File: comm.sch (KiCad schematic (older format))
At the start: 18 parts

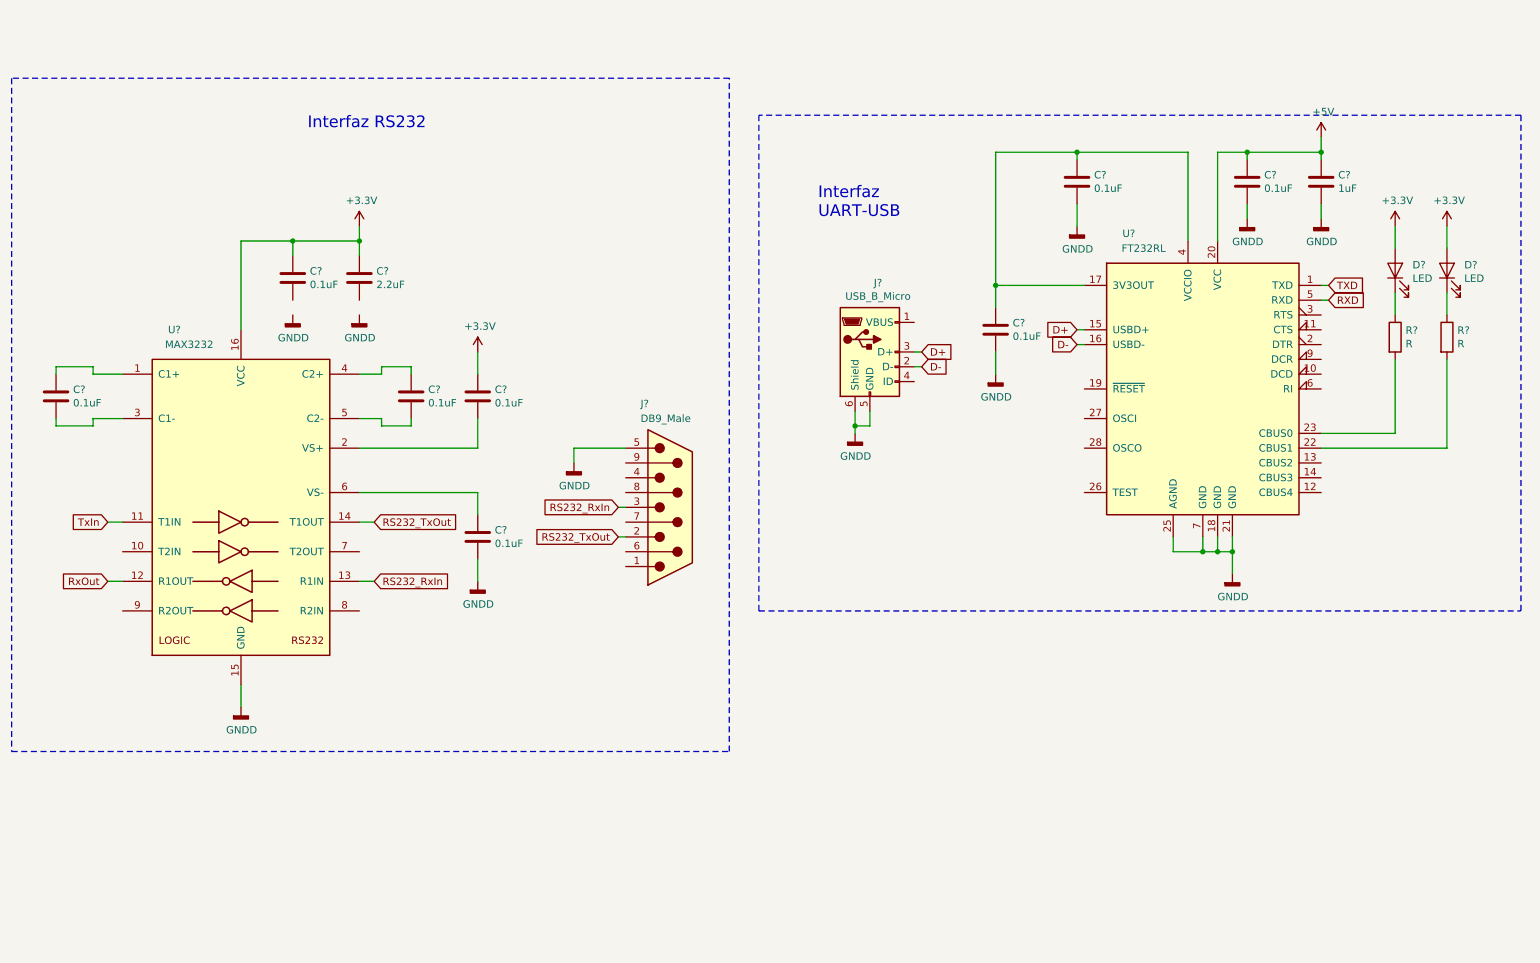
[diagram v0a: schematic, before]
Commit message: Se hace cambios en el esquematico y se anexa PCB
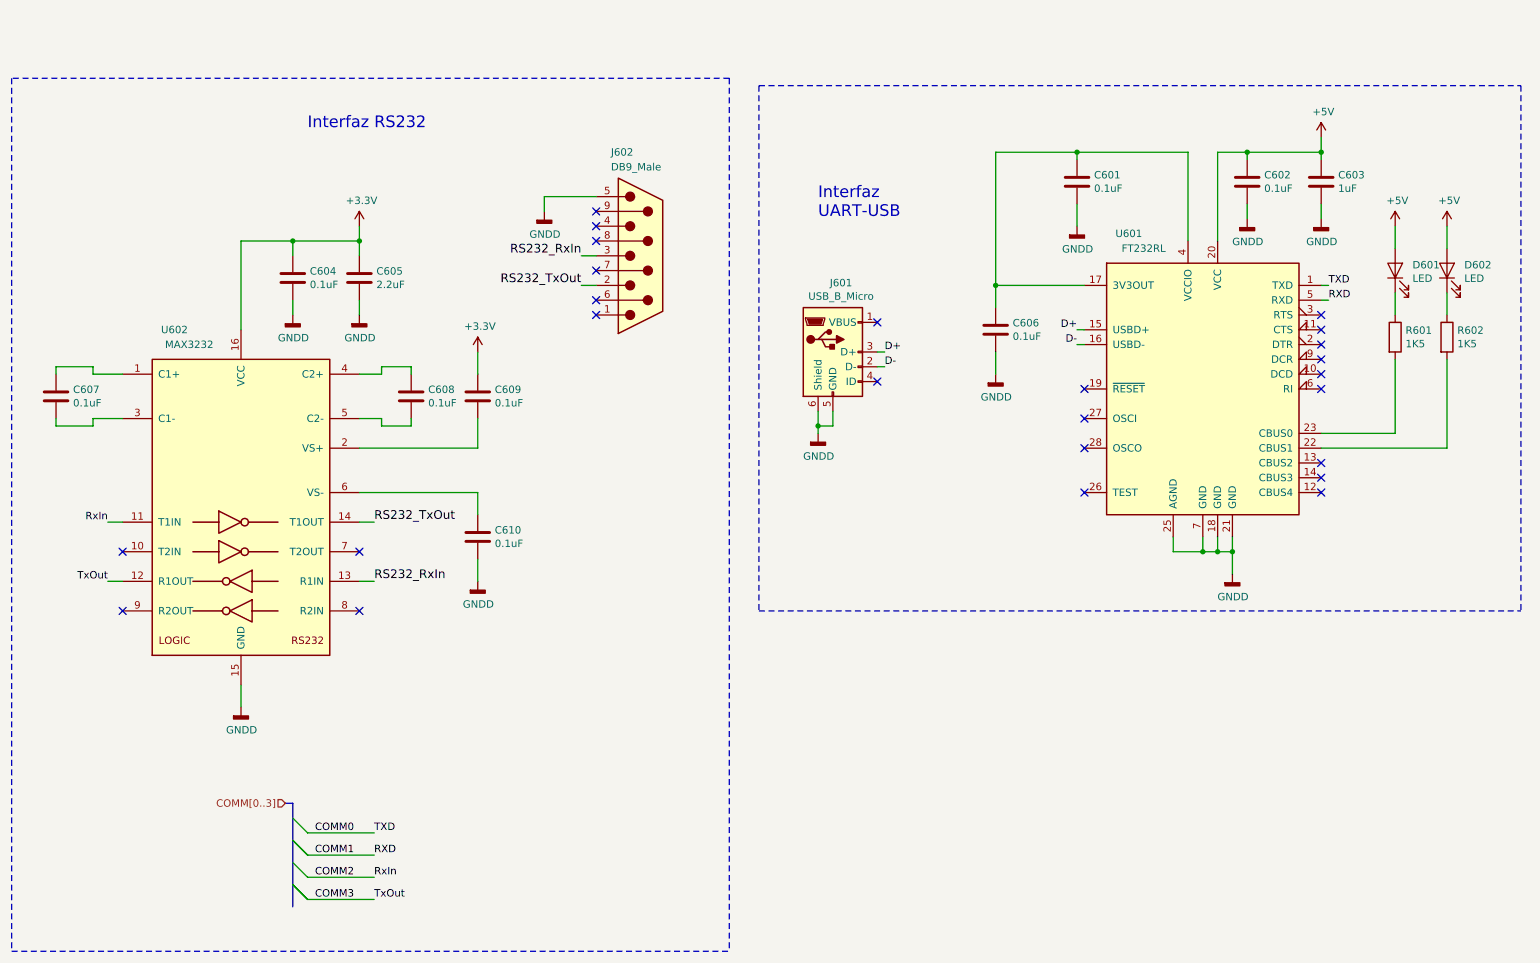
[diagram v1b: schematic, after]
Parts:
- C601, C602, C603, C604, C606, C607, C608, C609, C610: renamed from C?; footprint (none) -> Capacitor_SMD:C_0805_2012Metric_Pad1.15x1.40mm_HandSolder
- C605: renamed from C?; footprint (none) -> Capacitor_SMD:C_1206_3216Metric_Pad1.42x1.75mm_HandSolder
- D601, D602: renamed from D?; footprint (none) -> LED_SMD:LED_0805_2012Metric_Pad1.15x1.40mm_HandSolder
- J601: renamed from J?; footprint (none) -> Connector_USB:USB_Micro-B_Molex_47346-0001
- J602: renamed from J?; footprint (none) -> Connector_Dsub:DSUB-9_Male_Horizontal_P2.77x2.84mm_EdgePinOffset7.70mm_Housed_MountingHolesOffset9.12mm
- R601, R602: renamed from R?; value R -> 1K5; footprint (none) -> Resistor_SMD:R_0805_2012Metric_Pad1.15x1.40mm_HandSolder
- U602: renamed from U?; footprint (none) -> Package_SO:SOIC-16_3.9x9.9mm_P1.27mm
- gave numbers to parts that had none: 1
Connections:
- net +3V3: no longer D601.2 (A), D602.2 (A)
- net +5V: now also D601.2 (A), D602.2 (A)
- net GNDD: now also C604.2, C605.2
- net RXD renamed COMM1
- net RxOut renamed COMM3
- net TXD renamed COMM0
- net TxIn renamed COMM2
- no-connect marks 0 -> 25
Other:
- moved on the sheet: J601, J602

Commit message: Se realizan correcciones finales y se agregan carpetas BOM, Datasheet, Doc, Gerbers, lib.pretty y shapes3D
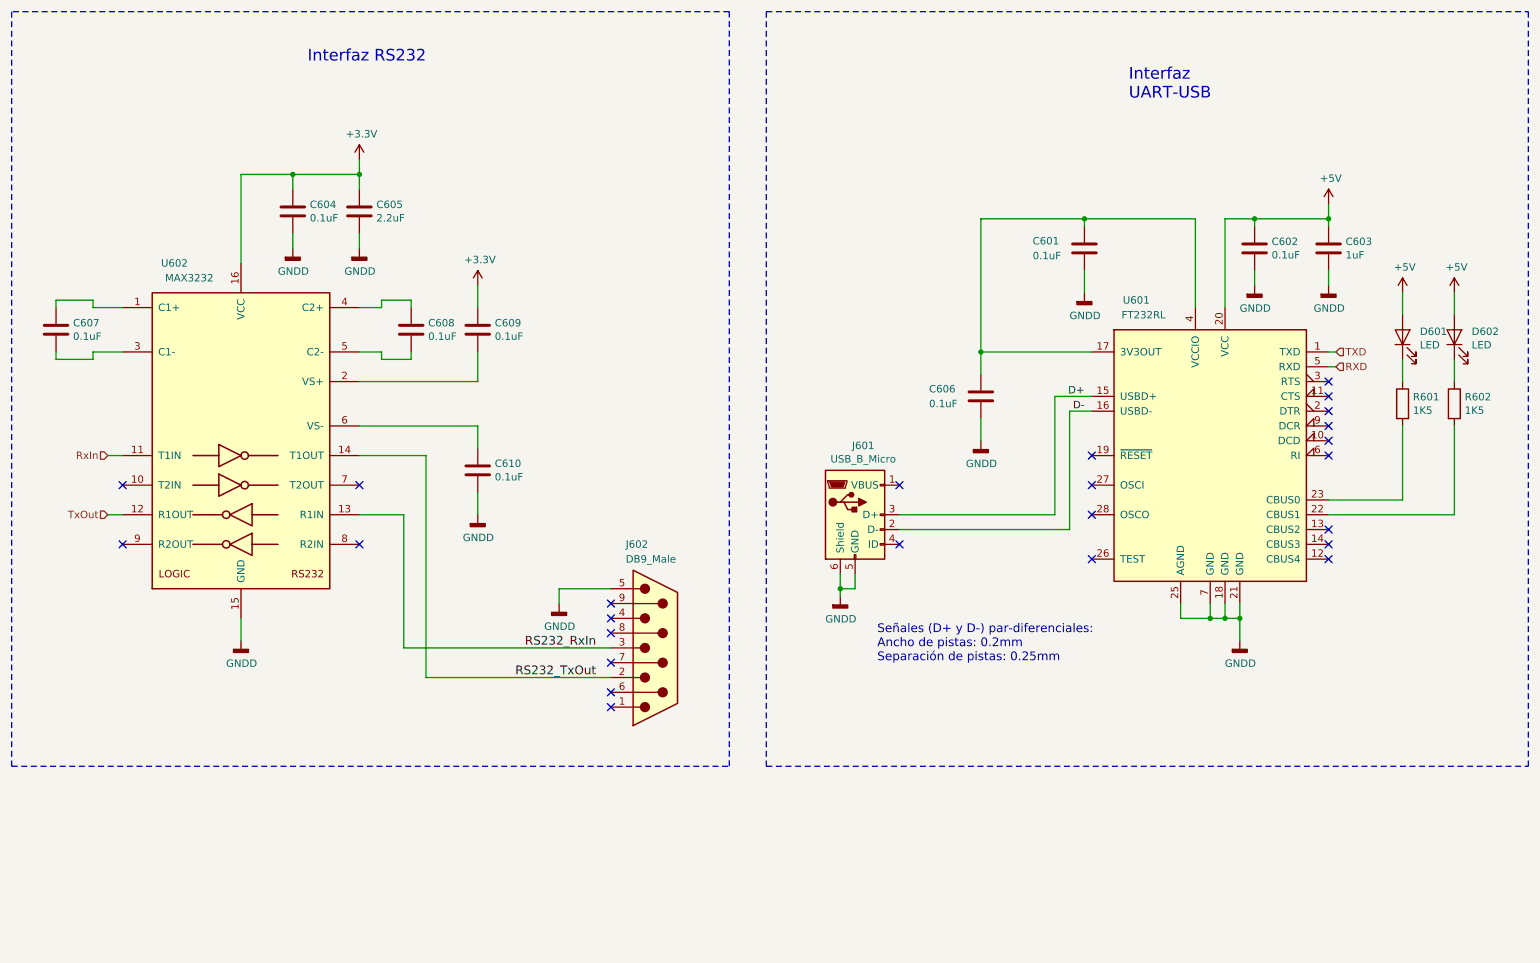
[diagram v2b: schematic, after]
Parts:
- J602: footprint Connector_Dsub:DSUB-9_Male_Horizontal_P2.77x2.84mm_EdgePinOffset7.70mm_Housed_MountingHolesOffset9.12mm -> Connector_Dsub:DSUB-9_Male_Horizontal_P2.77x2.84mm_EdgePinOffset4.94mm_Housed_MountingHolesOffset7.48mm
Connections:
- net COMM0 renamed TXD
- net COMM1 renamed RXD
- net COMM2 renamed RxIn
- net COMM3 renamed TxOut
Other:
- note added: "Señales (D+ y D-) par-diferenciales:\nAncho de pistas: 0.2mm\nSeparación de pistas: 0.25mm\n"
- moved on the sheet: C601, C602, C603, C604, C605, C606, C607, C608, C609, C610, D601, D602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
